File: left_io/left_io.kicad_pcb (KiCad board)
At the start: 8 copper layers, 70 x 185 mm, 266 parts, among them J190 AUX/SOLAR protected screw ter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, J21 USB-C dual-role data/PD port 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, J22 USB-C source-only data port J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, J23 USB-C source-only data port J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, J24 USB 3.0 Type-A internal heade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, J25 USB 2.0 Type-A internal heade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, Q15 SiSS4409DN 40V reverse-blocki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, Q16 SiSS4409DN 40V reverse-blocki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, Q17 SiSS4409DN 40V reverse-blocki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, Q18 SiSS4409DN 40V reverse-blocki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, Q2001 2N7002K DFP USB2 enable inver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, U14 LTC4418IUF#PBF dual-input PD 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, U1700 USB7206C-I/KDX six-port USB 3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, U1701 TPS62823DLC 3A USB7206C 1.146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, U1702 TLV803EA29 USB hub reset supe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, U1703 TPS56637RPAR VSYS to USB_PORT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, U1704 SN74LVC1G08 hub 3V3/core-PG r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, U1740 TPS2553DDBVR 1.3A USB branch, U1741 TPS25810RVCR Type-C DFP contr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, U1742 HD3SS6126RUAR USB3 orientatio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, U1743 TPD1S514-1YZR 5.9V VBUS OVP, U1745 TPD4E05U06 USB2/CC ESD, U1780 TPS2553DDBVR 1.3A USB branch, U1781 TPS25810RVCR Type-C DFP contr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, U1782 HD3SS6126RUAR USB3 orientatio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, U1783 TPD1S514-1YZR 5.9V VBUS OVP, U1785 TPD4E05U06 USB2/CC ESD, U1800 TPS2553DDBVR USB3-A VBUS bran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, U1801 USBLC6-2P6 USB3-A D+/D- ESD, U1802 TPD4E05U06 USB3-A SuperSpeed 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, U1803 TPS2553DDBVR USB2-A VBUS bran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, U1804 USBLC6-2P6 USB2-A D+/D- ESD, U2000 TUSB1142 USB 3.2 Gen 2 orient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, U2001 TPD4S201 CC and USB2 short-to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, U2002 CAT24C256 32KB private TPS257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, U2003 TS3USB30E DFP-qualified USB2 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, U2004 SN74LVC2G07 partial-power-dow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, U2005 TVS2200 22V USB VBUS surge cl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, U2006 SN74LVC1G08 DFP and attached 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, U41 TPS25751AD USB-PD DRP control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, U720 TPS26630RGER PD1 default-off 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, Y1700 25.000MHz 3.3V USB hub oscill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

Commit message: Board split Phase 4a: FPC connectors wired through the four split schematics
Connector symbols and sheets now exist in every project and the boundary
nets are pinned through them (same conductor order on both ends, verified
netlist-by-netlist):
  - gen/fpc_contract.py: authoritative FPC-1/2/3 pin maps + center-side
    renames (single source of truth for schematics, board pad nets, cable
    spec, and gate contracts)
  - gen/Conn_01x100_FFC_MP.kicad_sym (derived from the 30-pin pattern)
  - center: real fpc1_left/fpc2_right/fpc3_bms sheets wired to host pins
  - left_io/right_io: left_fpc/right_fpc connector sheets; bms carries
    FPC106 inline
  - connector refs FPC101..FPC106 (valid designators; FPC1_L-style refs
    broke KiCad annotation)
  - pack-rail naming reconciled: center gauge divider BAT_PROT_VIN ->
    PACK_POS_FUSED (same node as the BMS LTC4368 output); BMS ground
    /GND -> GND (pack negative is the system ground)

Boards: daughterboards re-synced from their connector-bearing schematics;
center connectors placed and their pad nets assigned text-side ((net
"name") convention).  Connector pads verified against every other
footprint (0 overlaps) and DRC shows 0 shorts on all four boards (center
16 pre-existing, down from 17).

Fixed two latent generator bugs exposed by the wiring:
  - resolve_connectors used naive +R rotation, placing Phase 3 connectors
    against mirrored phantom positions
  - pad half-extents were computed as footprint_rot+pad_rot, but KiCad
    saves pads with world orientation (FH12-100S pins are 1.3mm wide);
    both verified empirically against pcbnew, plus a connector-nudge pass
    for parts sandwiched between the connector body and pin columns

Gate: SCHEMATIC RELEASE CHECK: PASS (FPC pin contracts added per project;
closure audits 0 FAIL).  Routing remains manual (Phase 4b).
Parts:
- removed FPC1_L: FH12-100S-0.5SH_1x100-1MP_P0.50mm_Horizontal, ducktop2:FH12-100S-0.5SH_1x100-1MP_P0.50mm_Horizontal
- added FPC101: FH12-100S-0.5SH (FPC-1), ducktop2:FH12-100S-0.5SH_1x100-1MP_P0.50mm_Horizontal, F.Cu at (65.6, 130.5)
- moved R1840 54.0 mm to (8.00, 4.00)
- moved R1708 29.0 mm to (62.0, 2.00)
- moved U1702 15.0 mm to (39.0, 5.00)
- moved U1703 5.00 mm to (44.0, 5.00)
- moved U1701 4.12 mm to (24.0, 5.00)
- moved R2083 4.00 mm to (12.0, 4.00)
- moved R2084 4.00 mm to (16.0, 4.00)
- moved R2086 4.00 mm to (20.0, 4.00)

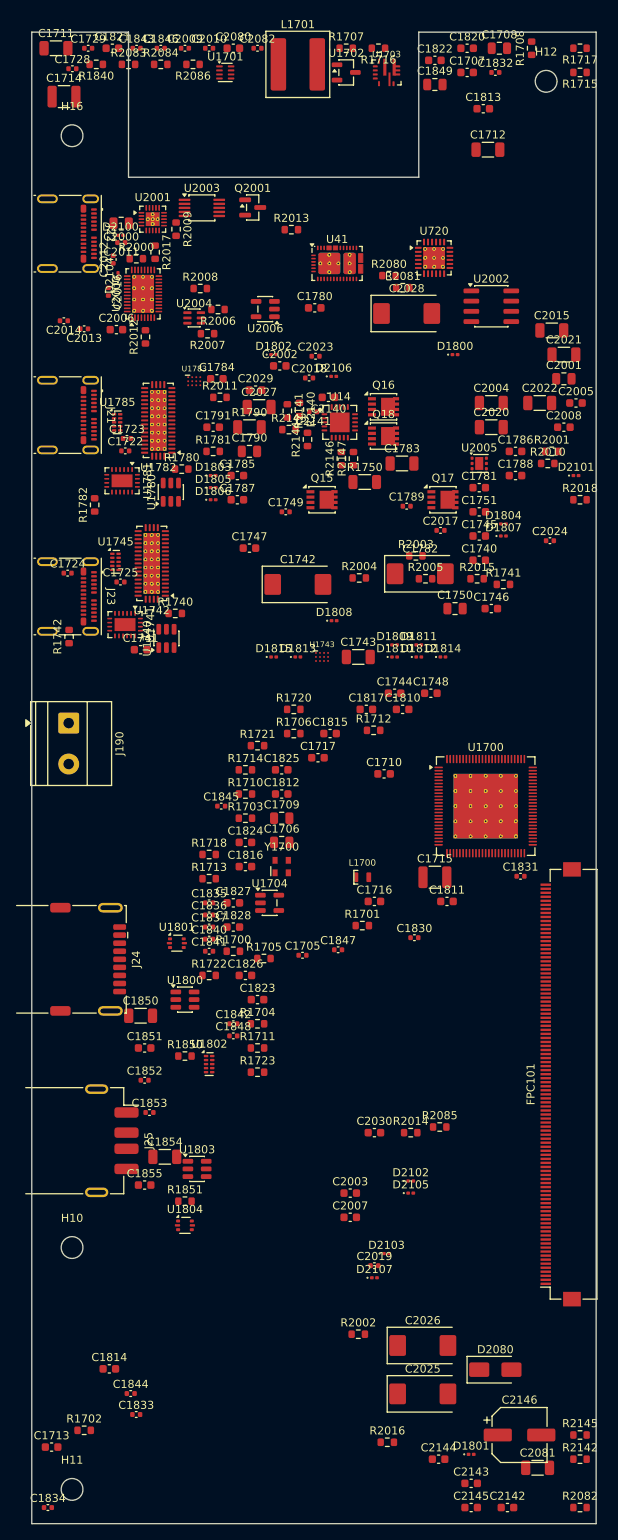
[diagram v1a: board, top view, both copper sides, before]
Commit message: Phase 4 deep audit: FH41-68S connectors, placement hygiene, one-shot fixes
Found and fixed four board-killers in the pre-fab audit:

1. Fictional connector: the Hirose FH12 series stops at 60 positions, so
   the 100-pin FH12-100S used for FPC-1/FPC-2 does not exist.  Replaced
   with the FH41-68S-0.5SH(05) (shielded-FFC, 68 positions; FPC-1 uses
   pins 1-53, FPC-2 pins 1-61):
   - new footprint derived from KiCad's FH41-30S (68 signal pads, MP at
     +/-18, 14 SH solder-holds, 38mm body) with SH pads tied to GND
   - new 68-pin symbol (Conn_01x68_FFC_MP), pin maps trimmed to 68
   - fictional FH12-100S footprint/symbol/script removed
   - cable spec updated (68-pin shielded FFC, one type for both)

2. Connector courtyard conflicts: parts sat under connector bodies
   (pads cleared, bodies collided).  Placement now enforces courtyard
   clearance against the connector body; the resolver scans with
   courtyard checks; a double-shift bug that hid re-placed parts' true
   positions was fixed.

3. FPC-3 orientation: the FH12's FPC enters from the +y side; both FPC-3
   connectors faced away from the seam.  FPC105 -> (123.5, 6.5) rot 180,
   FPC106 -> (30, 54) rot 0 so the cable exits the center bottom edge
   and enters the BMS top edge.

4. Original-layout defects: 16 genuine pad-pad shorts (inductor pads
   swallowing caps, passives on each other, parts on mounting holes) and
   23 parts inside the hinge cutouts (physically off the board) are all
   moved to legal spots; zones refilled against the final placement.

New post-build hygiene sweep (fix_board_hygiene.py) uses the final board
text as the geometry oracle, converges to a clean state, and reports
residuals instead of dropping them.

Final DRC: 0 shorts / 0 clearance / 0 hole violations on all four boards
(bms fully clean).  Remaining: courtyard touches around the Mu socket and
M.2 slot (design-inherent moat), chassis-edge copper, zone islands, silk
cosmetics, and unrouted nets (Phase 4b).  Gate: SCHEMATIC R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
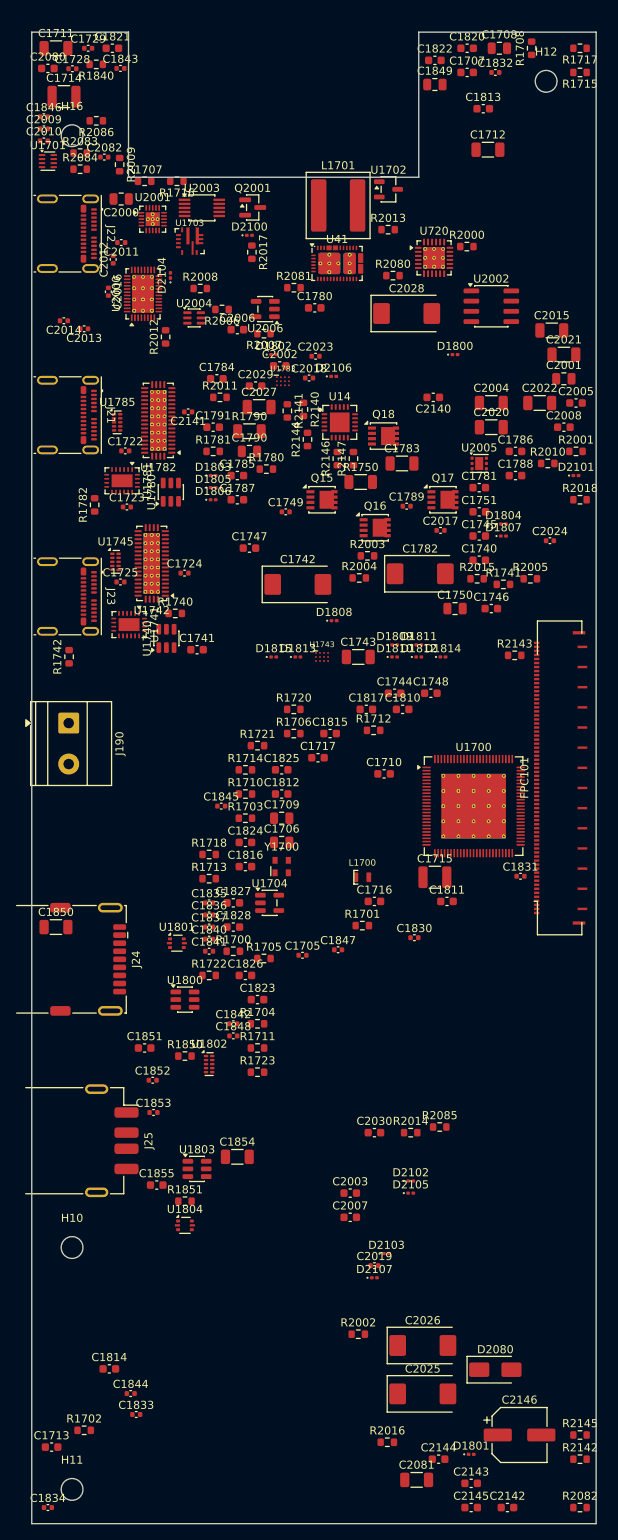
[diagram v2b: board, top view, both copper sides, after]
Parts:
- FPC101: value FH12-100S-0.5SH (FPC-1) -> FH41-68S-0.5SH (FPC-1); footprint ducktop2:FH12-100S-0.5SH_1x100-1MP_P0.50mm_Horizontal -> ducktop2:Hirose_FH41-68S-0.5SH_1x68_1MP_1SH_P0.5mm_Horizontal
- moved R2000 41.0 mm to (54.0, 26.6)
- moved R2143 39.6 mm to (59.9, 77.3)
- moved FPC101 38.0 mm to (65.6, 92.5)
- moved U1703 32.2 mm to (19.6, 25.9)
- moved R1707 30.0 mm to (14.0, 18.5)
- moved R1716 30.0 mm to (18.0, 18.5)
- moved U1701 24.6 mm to (2.00, 16.0)
- moved C2010 23.5 mm to (1.50, 13.5)
- moved C2082 23.3 mm to (9.00, 15.5)
- moved C2080 23.1 mm to (2.00, 4.50)
- moved C2009 20.2 mm to (1.50, 12.0)
- moved L1701 18.2 mm to (38.0, 21.5)
- moved C1846 16.8 mm to (1.50, 10.5)
- moved R2084 16.4 mm to (6.00, 17.0)
- moved D2100 16.0 mm to (27.0, 25.2)
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
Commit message: Phase 5: second-opinion audit remediation + rebuilt, verified board pipeline
Second-opinion AI audit found A-tier defects; remediation applied and the
board pipeline rebuilt on a known-good base with the fixes it needed:

- electrical: LTC4418IUF symbol pinout corrected (both selectors were
  dead as drawn); center charge cascade (U15 <- U15B, PD1 > PD2 > AUX);
  pack negative never crosses FPC-3, 15-pin FG_VSS return; power-budgeted
  FPC pin maps (0.4 A/pin derate); J12/DS4 completed; AUX source fuse
- FH41-68S footprint: 13 datasheet-correct SH pads + SH pin in symbol
- connector geometry settled against the Hirose FH12 2D drawing: FFC
  enters opposite the solder pins (mouth = local +Y); reversed side-B
  maps are correct for the 180-deg-mounted pairs; rotations set so mouths
  face across every seam
- pipeline (generate_split_boards.py): per-pin pad-net resync from the
  netlists (kills shadow nets for good), netlist-exact name
  normalization, netlist-only part injection (cascade, probe headers),
  zone refill after outline swap, read-before-write race fixed, orphan
  parts dropped loudly, non-zero exit on unresolved overlaps
- monolith board relocated to old/monolith_ducktop2.kicad_pcb (placement
  oracle for the center cut only)

verified end state: 4 boards 0 shorts / 0 clearance / 0 drill, 0 boundary
crossings, 6/6 connectors contract-exact with mouths facing, 0 shadow
nets, gates PASS x4, ERC 0 x4. routing next (499 nets/board).
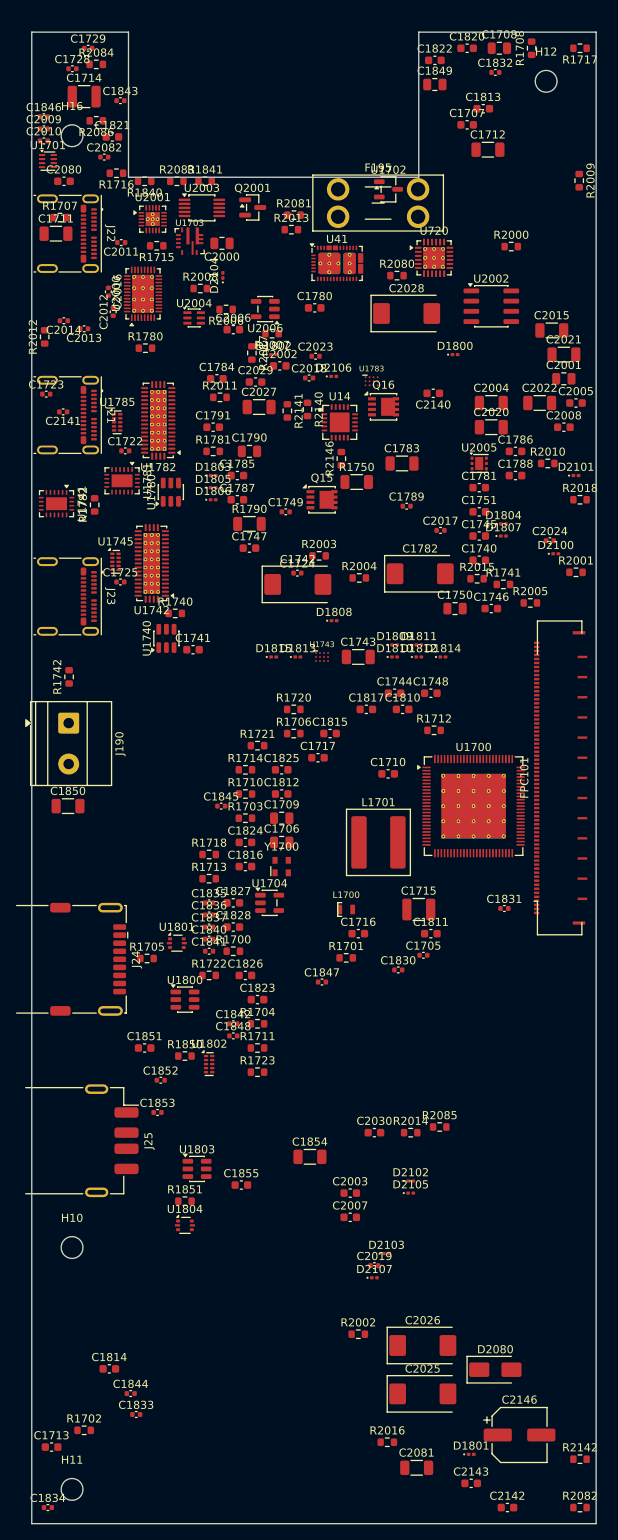
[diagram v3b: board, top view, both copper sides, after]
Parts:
- removed C2144, C2145: 100n 50V selector local, Capacitor_SMD:C_0603_1608Metric
- removed Q17, Q18: SiSS4409DN 40V reverse-blocking PMOS, Package_SO:Vishay_PowerPAK_1212-8_Single
- removed R2143: 1.00M 0.1% 15V UV top, Resistor_SMD:R_0603_1608Metric
- removed R2144: 19.6k 0.1% 15V window middle, Resistor_SMD:R_0603_1608Metric
- removed R2145: 63.4k 0.1% 15V OV bottom, Resistor_SMD:R_0603_1608Metric
- removed R2147: 10k PD2 VALID pull-up, Resistor_SMD:R_0603_1608Metric
- added F195: 3A MINI AUX source fuse: Littelfuse 0297003.WXNV, Fuse:Fuseholder_Blade_Mini_Keystone_3568, F.Cu at (38.0, 19.5)
- added R1841: 10k DS4 PRT_CTL idle pull-up (J12 branch enable, remote), Resistor_SMD:R_0603_1608Metric, F.Cu at (21.5, 18.5)
- H10, H11, H12, H16: value MountingHole_2.7mm_M2.5 -> M2.5 isolated mainboard mounting hole
- U14: value LTC4418IUF#PBF dual-input PD selector -> LTC4418IUF#PBF dual-input PD selector (V1 = J21)
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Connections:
- net HUB_3V3_OK renamed /USB Hub + Ports/HUB_3V3_OK
- net HUB_BC_EN renamed /USB Hub + Ports/HUB_BC_EN
- net HUB_CFG1 renamed /USB Hub + Ports/HUB_CFG1
- net HUB_CFG2 renamed /USB Hub + Ports/HUB_CFG2
- net HUB_CFG3 renamed /USB Hub + Ports/HUB_CFG3
- net HUB_CLK renamed /USB Hub + Ports/HUB_CLK
- net HUB_CORE_FB renamed /USB Hub + Ports/HUB_CORE_FB
- net HUB_CORE_PG renamed /USB Hub + Ports/HUB_CORE_PG
- net HUB_CORE_SW renamed /USB Hub + Ports/HUB_CORE_SW
- net HUB_DIS5_DM renamed /USB Hub + Ports/HUB_DIS5_DM
- net HUB_DIS5_DP renamed /USB Hub + Ports/HUB_DIS5_DP
- net HUB_DIS5_RX_N renamed /USB Hub + Ports/HUB_DIS5_RX_N
- net HUB_DIS5_RX_P renamed /USB Hub + Ports/HUB_DIS5_RX_P
- net HUB_DIS5_TX_N renamed /USB Hub + Ports/HUB_DIS5_TX_N
- net HUB_DIS5_TX_P renamed /USB Hub + Ports/HUB_DIS5_TX_P
- net HUB_DIS6_DM renamed /USB Hub + Ports/HUB_DIS6_DM
- net HUB_DIS6_DP renamed /USB Hub + Ports/HUB_DIS6_DP
- net HUB_DS1_PRT_CTL renamed /USB Hub + Ports/HUB_DS1_PRT_CTL
- net HUB_DS2_DM renamed /USB Hub + Ports/HUB_DS2_DM
- net HUB_DS2_DP renamed /USB Hub + Ports/HUB_DS2_DP
- net HUB_DS2_SSRX_N renamed /USB Hub + Ports/HUB_DS2_SSRX_N
- net HUB_DS2_SSRX_P renamed /USB Hub + Ports/HUB_DS2_SSRX_P
- net HUB_DS2_SSTX_N renamed /USB Hub + Ports/HUB_DS2_SSTX_N
- net HUB_DS2_SSTX_P renamed /USB Hub + Ports/HUB_DS2_SSTX_P
- net HUB_DS2_TX_RAW_N renamed /USB Hub + Ports/HUB_DS2_TX_RAW_N
- net HUB_DS2_TX_RAW_P renamed /USB Hub + Ports/HUB_DS2_TX_RAW_P
- net HUB_DS3_DM renamed /USB Hub + Ports/HUB_DS3_DM
- net HUB_DS3_DP renamed /USB Hub + Ports/HUB_DS3_DP
- net HUB_DS3_SSRX_N renamed /USB Hub + Ports/HUB_DS3_SSRX_N
- net HUB_DS3_SSRX_P renamed /USB Hub + Ports/HUB_DS3_SSRX_P
- net HUB_DS3_SSTX_N renamed /USB Hub + Ports/HUB_DS3_SSTX_N
- net HUB_DS3_SSTX_P renamed /USB Hub + Ports/HUB_DS3_SSTX_P
- net HUB_DS3_TX_RAW_N renamed /USB Hub + Ports/HUB_DS3_TX_RAW_N
- net HUB_DS3_TX_RAW_P renamed /USB Hub + Ports/HUB_DS3_TX_RAW_P
- net HUB_NON_REM renamed /USB Hub + Ports/HUB_NON_REM
- net HUB_PRT_CTL2 renamed /USB Hub + Ports/HUB_PRT_CTL2
- net HUB_PRT_CTL3 renamed /USB Hub + Ports/HUB_PRT_CTL3
- net HUB_RBIAS renamed /USB Hub + Ports/HUB_RBIAS
- net HUB_RESET_N renamed /USB Hub + Ports/HUB_RESET_N
- net HUB_SPI_CLK renamed /USB Hub + Ports/HUB_SPI_CLK
- net HUB_SPI_D1 renamed /USB Hub + Ports/HUB_SPI_D1
- net HUB_SPI_D2 renamed /USB Hub + Ports/HUB_SPI_D2
- net HUB_SPI_D3 renamed /USB Hub + Ports/HUB_SPI_D3
- net HUB_TEST1 renamed /USB Hub + Ports/HUB_TEST1
- net HUB_TEST2 renamed /USB Hub + Ports/HUB_TEST2
- net HUB_TEST3 renamed /USB Hub + Ports/HUB_TEST3
- net HUB_UP_TX_RAW_N renamed /USB Hub + Ports/HUB_UP_TX_RAW_N
- net HUB_UP_TX_RAW_P renamed /USB Hub + Ports/HUB_UP_TX_RAW_P
- net HUB_VCORE renamed /USB Hub + Ports/HUB_VCORE
- net J22_5V_PRE renamed /USB Hub + Ports/J22_5V_PRE
- net J22_CC1 renamed /USB Hub + Ports/J22_CC1
- net J22_CC2 renamed /USB Hub + Ports/J22_CC2
- net J22_ILIM renamed /USB Hub + Ports/J22_ILIM
- net J22_POL_N renamed /USB Hub + Ports/J22_POL_N
- net J22_REF renamed /USB Hub + Ports/J22_REF
- net J22_REF_RTN renamed /USB Hub + Ports/J22_REF_RTN
- net J22_RX1_N renamed /USB Hub + Ports/J22_RX1_N
- net J22_RX1_P renamed /USB Hub + Ports/J22_RX1_P
- net J22_RX2_N renamed /USB Hub + Ports/J22_RX2_N
- net J22_RX2_P renamed /USB Hub + Ports/J22_RX2_P
- net J22_TX1_N renamed /USB Hub + Ports/J22_TX1_N
- net J22_TX1_P renamed /USB Hub + Ports/J22_TX1_P
- net J22_TX2_N renamed /USB Hub + Ports/J22_TX2_N
- net J22_TX2_P renamed /USB Hub + Ports/J22_TX2_P
- net J22_VBUS renamed /USB Hub + Ports/J22_VBUS
- net J22_VBUS_POWER renamed /USB Hub + Ports/J22_VBUS_POWER
- net J22_VBUS_SYS renamed /USB Hub + Ports/J22_VBUS_SYS
- net J23_5V_PRE renamed /USB Hub + Ports/J23_5V_PRE
- net J23_CC1 renamed /USB Hub + Ports/J23_CC1
- net J23_CC2 renamed /USB Hub + Ports/J23_CC2
- net J23_ILIM renamed /USB Hub + Ports/J23_ILIM
- net J23_POL_N renamed /USB Hub + Ports/J23_POL_N
- net J23_REF renamed /USB Hub + Ports/J23_REF
- net J23_REF_RTN renamed /USB Hub + Ports/J23_REF_RTN
- net J23_RX1_N renamed /USB Hub + Ports/J23_RX1_N
- net J23_RX1_P renamed /USB Hub + Ports/J23_RX1_P
- net J23_RX2_N renamed /USB Hub + Ports/J23_RX2_N
- net J23_RX2_P renamed /USB Hub + Ports/J23_RX2_P
- net J23_TX1_N renamed /USB Hub + Ports/J23_TX1_N
- net J23_TX1_P renamed /USB Hub + Ports/J23_TX1_P
- net J23_TX2_N renamed /USB Hub + Ports/J23_TX2_N
- net J23_TX2_P renamed /USB Hub + Ports/J23_TX2_P
- net J23_VBUS renamed /USB Hub + Ports/J23_VBUS
- net J23_VBUS_POWER renamed /USB Hub + Ports/J23_VBUS_POWER
- net J23_VBUS_SYS renamed /USB Hub + Ports/J23_VBUS_SYS
- net J24_5V_PRE renamed /USB Hub + Ports/J24_5V_PRE
- net J24_ILIM renamed /USB Hub + Ports/J24_ILIM
- net J24_SSTX_N renamed /USB Hub + Ports/J24_SSTX_N
- net J24_SSTX_P renamed /USB Hub + Ports/J24_SSTX_P
- net J25_5V_PRE renamed /USB Hub + Ports/J25_5V_PRE
- net J25_ILIM renamed /USB Hub + Ports/J25_ILIM
- net PD1_CC1_CONN renamed /PD1 Dual-Role/PD1_CC1_CONN
- net PD1_CC1_SYS renamed /PD1 Dual-Role/PD1_CC1_SYS
- net PD1_CC2_CONN renamed /PD1 Dual-Role/PD1_CC2_CONN
- net PD1_CC2_SYS renamed /PD1 Dual-Role/PD1_CC2_SYS
- net PD1_CC_ESD_VBIAS renamed /PD1 Dual-Role/PD1_CC_ESD_VBIAS
- net PD1_CC_FAULT_LOCAL_N renamed /PD1 Dual-Role/PD1_CC_FAULT_LOCAL_N
- net PD1_CTX1_RAW_N renamed /PD1 Dual-Role/PD1_CTX1_RAW_N
- net PD1_CTX1_RAW_P renamed /PD1 Dual-Role/PD1_CTX1_RAW_P
- net PD1_CTX2_RAW_N renamed /PD1 Dual-Role/PD1_CTX2_RAW_N
- net PD1_CTX2_RAW_P renamed /PD1 Dual-Role/PD1_CTX2_RAW_P
- net PD1_DM_CONN renamed /PD1 Dual-Role/PD1_DM_CONN
- net PD1_DM_HOST_SWITCHED renamed /PD1 Dual-Role/PD1_DM_HOST_SWITCHED
- net PD1_DP_CONN renamed /PD1 Dual-Role/PD1_DP_CONN
- net PD1_DP_HOST_SWITCHED renamed /PD1 Dual-Role/PD1_DP_HOST_SWITCHED
- net PD1_DRAIN_THERMAL renamed /PD1 Dual-Role/PD1_DRAIN_THERMAL
- net PD1_EEPROM_IRQ_N renamed /PD1 Dual-Role/PD1_EEPROM_IRQ_N
- net PD1_EEPROM_SCL renamed /PD1 Dual-Role/PD1_EEPROM_SCL
- net PD1_EEPROM_SDA renamed /PD1 Dual-Role/PD1_EEPROM_SDA
- net PD1_EFUSE_DVDT renamed /PD1 Dual-Role/PD1_EFUSE_DVDT
- net PD1_EFUSE_ILIM renamed /PD1 Dual-Role/PD1_EFUSE_ILIM
- net PD1_EFUSE_OV renamed /PD1 Dual-Role/PD1_EFUSE_OV
- net PD1_EFUSE_SHDN renamed /PD1 Dual-Role/PD1_EFUSE_SHDN
- net PD1_EFUSE_UV renamed /PD1 Dual-Role/PD1_EFUSE_UV
- net PD1_GPIO_ATTACH renamed /PD1 Dual-Role/PD1_GPIO_ATTACH
- net PD1_GPIO_DFP renamed /PD1 Dual-Role/PD1_GPIO_DFP
- net PD1_GPIO_FLIP renamed /PD1 Dual-Role/PD1_GPIO_FLIP
- net PD1_HOST_ATTACHED renamed /PD1 Dual-Role/PD1_HOST_ATTACHED
- net PD1_LDO1V5 renamed /PD1 Dual-Role/PD1_LDO1V5
- net PD1_LDO3V3 renamed /PD1 Dual-Role/PD1_LDO3V3
- net PD1_MUX_EN renamed /PD1 Dual-Role/PD1_MUX_EN
- net PD1_MUX_EQCFG renamed /PD1 Dual-Role/PD1_MUX_EQCFG
- net PD1_MUX_FLIP renamed /PD1 Dual-Role/PD1_MUX_FLIP
- net PD1_MUX_MODE renamed /PD1 Dual-Role/PD1_MUX_MODE
- net PD1_MUX_SLEEP_N renamed /PD1 Dual-Role/PD1_MUX_SLEEP_N
- net PD1_MUX_SSEQ1 renamed /PD1 Dual-Role/PD1_MUX_SSEQ1
- net PD1_MUX_VIO renamed /PD1 Dual-Role/PD1_MUX_VIO
- net PD1_PPHV renamed /PD1 Dual-Role/PD1_PPHV
- net PD1_RX1_N renamed /PD1 Dual-Role/PD1_RX1_N
- net PD1_RX1_P renamed /PD1 Dual-Role/PD1_RX1_P
- net PD1_RX2_N renamed /PD1 Dual-Role/PD1_RX2_N
- net PD1_RX2_P renamed /PD1 Dual-Role/PD1_RX2_P
- net PD1_SEL_FET_COMMON renamed /PD1 Dual-Role/PD1_SEL_FET_COMMON
- net PD1_SEL_GATE renamed /PD1 Dual-Role/PD1_SEL_GATE
- net PD1_SEL_OV renamed /PD1 Dual-Role/PD1_SEL_OV
- net PD1_SEL_UV renamed /PD1 Dual-Role/PD1_SEL_UV
- net PD1_SSRX_RAW_N renamed /PD1 Dual-Role/PD1_SSRX_RAW_N
- net PD1_SSRX_RAW_P renamed /PD1 Dual-Role/PD1_SSRX_RAW_P
- net PD1_TX1_N renamed /PD1 Dual-Role/PD1_TX1_N
- net PD1_TX1_P renamed /PD1 Dual-Role/PD1_TX1_P
- net PD1_TX2_N renamed /PD1 Dual-Role/PD1_TX2_N
- net PD1_TX2_P renamed /PD1 Dual-Role/PD1_TX2_P
- net PD1_USB2_OE_N renamed /PD1 Dual-Role/PD1_USB2_OE_N
- net PD1_VBUS_GATED renamed /PD1 Dual-Role/PD1_VBUS_GATED
- net PD_SEL_TMR renamed /PD1 Dual-Role/PD_SEL_TMR
- net USB5_BOOT renamed /USB Hub + Ports/USB5_BOOT
- net USB5_EN renamed /USB Hub + Ports/USB5_EN
- net USB5_FB renamed /USB Hub + Ports/USB5_FB
- net USB5_PG renamed /USB Hub + Ports/USB5_PG
- net USB5_SW renamed /USB Hub + Ports/USB5_SW
- C1706 pad 1: SYS_3V3 -> /SYS_3V3
- C1707 pad 1: SYS_3V3 -> /SYS_3V3
- C1711 pad 1: VSYS -> /VSYS
- C1712 pad 1: VSYS -> /VSYS
- C1713 pad 1: VSYS -> /VSYS
- C1714 pad 1: USB_PORT_5V -> /USB_PORT_5V
- C1715 pad 1: USB_PORT_5V -> /USB_PORT_5V
- C1716 pad 1: SYS_3V3 -> /SYS_3V3
- C1717 pad 1: SYS_3V3 -> /SYS_3V3
- C1728 pad 2: USBC2_SSRX_P -> /USBC2_SSRX_P
- C1729 pad 2: USBC2_SSRX_N -> /USBC2_SSRX_N
- C1740 pad 1: USB_PORT_5V -> /USB_PORT_5V
- C1744 pad 1: SYS_3V3 -> /SYS_3V3
- C1745 pad 1: SYS_3V3 -> /SYS_3V3
- C1746 pad 1: SYS_3V3 -> /SYS_3V3
- C1747 pad 1: SYS_3V3 -> /SYS_3V3
- C1748 pad 1: SYS_3V3 -> /SYS_3V3
- C1749 pad 1: SYS_3V3 -> /SYS_3V3
- C1780 pad 1: USB_PORT_5V -> /USB_PORT_5V
- C1784 pad 1: SYS_3V3 -> /SYS_3V3
- C1785 pad 1: SYS_3V3 -> /SYS_3V3
- C1786 pad 1: SYS_3V3 -> /SYS_3V3
- C1787 pad 1: SYS_3V3 -> /SYS_3V3
- C1788 pad 1: SYS_3V3 -> /SYS_3V3
- C1789 pad 1: SYS_3V3 -> /SYS_3V3
- C1810 pad 1: SYS_3V3 -> /SYS_3V3
- C1811 pad 1: SYS_3V3 -> /SYS_3V3
- C1812 pad 1: SYS_3V3 -> /SYS_3V3
- C1813 pad 1: SYS_3V3 -> /SYS_3V3
- C1814 pad 1: SYS_3V3 -> /SYS_3V3
- C1815 pad 1: SYS_3V3 -> /SYS_3V3
- C1816 pad 1: SYS_3V3 -> /SYS_3V3
- C1817 pad 1: SYS_3V3 -> /SYS_3V3
- C1830 pad 1: SYS_3V3 -> /SYS_3V3
- C1831 pad 1: SYS_3V3 -> /SYS_3V3
- C1832 pad 1: SYS_3V3 -> /SYS_3V3
- C1833 pad 1: SYS_3V3 -> /SYS_3V3
- C1834 pad 1: SYS_3V3 -> /SYS_3V3
- C1835 pad 1: SYS_3V3 -> /SYS_3V3
- C1836 pad 1: SYS_3V3 -> /SYS_3V3
- C1837 pad 1: SYS_3V3 -> /SYS_3V3
- C1849 pad 1: SYS_3V3 -> /SYS_3V3
- C2003 pad 1: SYS_3V3 -> /SYS_3V3
- C2004 pad 1: SYS_3V3 -> /SYS_3V3
- C2005 pad 1: SYS_3V3 -> /SYS_3V3
- C2006 pad 1: SYS_3V3 -> /SYS_3V3
- C2007 pad 1: SYS_3V3 -> /SYS_3V3
- C2008 pad 1: SYS_3V3 -> /SYS_3V3
- C2009 pad 2: USBC1_SSRX_P -> /USBC1_SSRX_P
- C2010 pad 2: USBC1_SSRX_N -> /USBC1_SSRX_N
- C2015 pad 1: PD1_VBUS_RAW -> /PD1_VBUS_RAW
- C2016 pad 1: PD1_VBUS_RAW -> /PD1_VBUS_RAW
- C2017 pad 1: PD1_VBUS_RAW -> /PD1_VBUS_RAW
- C2018 pad 1: PD1_VBUS_RAW -> /PD1_VBUS_RAW
- C2019 pad 1: PD1_VBUS_RAW -> /PD1_VBUS_RAW
- C2022 pad 1: MCU_3V3 -> /MCU_3V3
- C2025 pad 1: USB_PORT_5V -> /USB_PORT_5V
- C2026 pad 1: USB_PORT_5V -> /USB_PORT_5V
- C2027 pad 1: USB_PORT_5V -> /USB_PORT_5V
- C2030 pad 1: SYS_3V3 -> /SYS_3V3
- C2140 pad 1: PD_SEL_INTVCC -> /PD1 Dual-Role/PD_SEL_INTVCC
- C2146 pad 1: USB_PD_SELECTED -> /USB_PD_SELECTED
- FPC101 pad 1: VSYS -> /VSYS
- FPC101 pad 10: GND -> /USB_PORT_5V
- FPC101 pad 11: PD1_VBUS_RAW -> /USB_PORT_5V
- FPC101 pad 12: GND -> /USB_PORT_5V
- FPC101 pad 13: AUX_DC_RAW -> GND
- FPC101 pad 14: GND -> /SYS_3V3
- FPC101 pad 15: USB_PD_SELECTED -> /SYS_3V3
- FPC101 pad 16: GND -> /MCU_3V3
- FPC101 pad 17: INTERNAL_USB_VBUS_VALID -> /PD1_VBUS_RAW
- FPC101 pad 18: GND -> /PD1_VBUS_RAW
- FPC101 pad 19: PD1_I2C_SCL -> /PD1_VBUS_RAW
- FPC101 pad 2: VSYS -> /VSYS
- FPC101 pad 20: PD1_I2C_SDA -> /PD1_VBUS_RAW
- FPC101 pad 21: GND -> /PD1_VBUS_RAW
- FPC101 pad 22: PD1_TCPC_IRQ_N -> /PD1_VBUS_RAW
- FPC101 pad 23: GND -> /USB_PD_SELECTED
- FPC101 pad 24: PD1_PATH_EN -> /USB_PD_SELECTED
- FPC101 pad 25: GND -> /USB_PD_SELECTED
- FPC101 pad 26: PD1_VALID_N -> /USB_PD_SELECTED
- FPC101 pad 27: GND -> /USB_PD_SELECTED
- FPC101 pad 28: PD2_VALID_N -> /USB_PD_SELECTED
- FPC101 pad 29: GND -> /AUX_DC_RAW
- FPC101 pad 3: GND -> /VSYS
- FPC101 pad 30: PD1_EFUSE_FAULT_N -> /AUX_DC_RAW
- FPC101 pad 31: GND -> /AUX_DC_RAW
- FPC101 pad 32: PD_PROTECT_FAULT_N -> /AUX_DC_RAW
- FPC101 pad 33: GND -> /AUX_DC_RAW
- FPC101 pad 34: USBC1_DP -> /AUX_DC_RAW
- FPC101 pad 35: USBC1_DM -> GND
- FPC101 pad 37: USBC2_DP -> GND
- FPC101 pad 38: USBC2_DM -> /INTERNAL_USB_VBUS_VALID
- FPC101 pad 39: GND -> /PD1_I2C_SCL
- FPC101 pad 4: USB_PORT_5V -> /VSYS
- FPC101 pad 40: HUB_DS1_DP -> /PD1_I2C_SDA
- FPC101 pad 41: HUB_DS1_DM -> /PD1_TCPC_IRQ_N
- FPC101 pad 42: GND -> /PD1_PATH_EN
- FPC101 pad 43: USBC1_SSRX_P -> /PD1_VALID_N
- FPC101 pad 44: USBC1_SSRX_N -> /PD1_EFUSE_FAULT_N
- FPC101 pad 45: GND -> /PD_PROTECT_FAULT_N
- FPC101 pad 46: USBC1_SSTX_P -> /HUB_DS4_DP
- FPC101 pad 47: USBC1_SSTX_N -> /HUB_DS4_DM
- FPC101 pad 48: GND -> /HUB_PRT_CTL4
- FPC101 pad 49: USBC2_SSRX_P -> /USBC1_DP
- FPC101 pad 5: USB_PORT_5V -> /VSYS
- FPC101 pad 50: USBC2_SSRX_N -> /USBC1_DM
- FPC101 pad 52: USBC2_SSTX_P -> /USBC2_DP
- FPC101 pad 53: USBC2_SSTX_N -> /USBC2_DM
- FPC101 pad 55: GND -> /HUB_DS1_DP
- FPC101 pad 56: GND -> /HUB_DS1_DM
- FPC101 pad 58: GND -> /USBC1_SSRX_P
- FPC101 pad 59: GND -> /USBC1_SSRX_N
- FPC101 pad 6: GND -> /VSYS
- FPC101 pad 61: GND -> /USBC1_SSTX_P
- FPC101 pad 62: GND -> /USBC1_SSTX_N
- FPC101 pad 64: GND -> /USBC2_SSRX_P
- FPC101 pad 65: GND -> /USBC2_SSRX_N
- FPC101 pad 66: GND -> /USBC2_SSTX_P
- FPC101 pad 67: GND -> /USBC2_SSTX_N
- FPC101 pad 7: SYS_3V3 -> GND
- FPC101 pad 9: MCU_3V3 -> /USB_PORT_5V
- J190 pad 1: AUX_DC_RAW -> /PD1 Dual-Role/AUX_DC_TERM
- J21 pad A4: PD1_VBUS_RAW -> /PD1_VBUS_RAW
- J21 pad A8: (no net) -> unconnected-(J21-SBU1-PadA8)
- J21 pad A9: PD1_VBUS_RAW -> /PD1_VBUS_RAW
- J21 pad B4: PD1_VBUS_RAW -> /PD1_VBUS_RAW
- J21 pad B8: (no net) -> unconnected-(J21-SBU2-PadB8)
- J21 pad B9: PD1_VBUS_RAW -> /PD1_VBUS_RAW
- J22 pad A8: (no net) -> unconnected-(J22-SBU1-PadA8)
- J22 pad B8: (no net) -> unconnected-(J22-SBU2-PadB8)
- J23 pad A8: (no net) -> unconnected-(J23-SBU1-PadA8)
- J23 pad B8: (no net) -> unconnected-(J23-SBU2-PadB8)
- L1701 pad 2: USB_PORT_5V -> /USB_PORT_5V
- Q16 pad 5: USB_PD_SELECTED -> /USB_PD_SELECTED
- R1707 pad 1: SYS_3V3 -> /SYS_3V3
- R1710 pad 1: VSYS -> /VSYS
- R1712 pad 1: USB_PORT_5V -> /USB_PORT_5V
- R1714 pad 1: SYS_3V3 -> /SYS_3V3
- R1715 pad 1: SYS_3V3 -> /SYS_3V3
- R1716 pad 1: SYS_3V3 -> /SYS_3V3
- R1717 pad 1: SYS_3V3 -> /SYS_3V3
- R1718 pad 1: SYS_3V3 -> /SYS_3V3
- R1741 pad 1: SYS_3V3 -> /SYS_3V3
- R1781 pad 1: SYS_3V3 -> /SYS_3V3
- R1840 pad 1: SYS_3V3 -> /SYS_3V3
- R2000 pad 1: MCU_3V3 -> /MCU_3V3
- R2000 pad 2: PD_PROTECT_FAULT_N -> /PD_PROTECT_FAULT_N
- R2003 pad 1: MCU_3V3 -> /MCU_3V3
- R2003 pad 2: PD1_I2C_SDA -> /PD1_I2C_SDA
- R2004 pad 1: MCU_3V3 -> /MCU_3V3
- R2004 pad 2: PD1_I2C_SCL -> /PD1_I2C_SCL
- R2005 pad 1: MCU_3V3 -> /MCU_3V3
- R2005 pad 2: PD1_TCPC_IRQ_N -> /PD1_TCPC_IRQ_N
- R2006 pad 1: SYS_3V3 -> /SYS_3V3
- R2007 pad 1: SYS_3V3 -> /SYS_3V3
- R2012 pad 1: SYS_3V3 -> /SYS_3V3
- R2016 pad 1: SYS_3V3 -> /SYS_3V3
- R2017 pad 2: PD_PROTECT_FAULT_N -> /PD_PROTECT_FAULT_N
- R2085 pad 1: PD1_PATH_EN -> /PD1_PATH_EN
- R2086 pad 1: MCU_3V3 -> /MCU_3V3
- R2086 pad 2: PD1_EFUSE_FAULT_N -> /PD1_EFUSE_FAULT_N
- R2146 pad 1: MCU_3V3 -> /MCU_3V3
- R2146 pad 2: PD1_VALID_N -> /PD1_VALID_N
- U14 pad 10: PD2_VALID_N -> /PD1 Dual-Role/PD_SEL_INTVCC
- U14 pad 11: PD2_SEL_GATE -> unconnected-(U14-G2-Pad11)
- U14 pad 12: PD2_SEL_FET_COMMON -> GND
- U14 pad 15: USB_PD_SELECTED -> /USB_PD_SELECTED
- U14 pad 16: PD2_VBUS_GATED -> GND
- U14 pad 18: PD_SEL_INTVCC -> /PD1 Dual-Role/PD_SEL_INTVCC
- U14 pad 19: PD_SEL_INTVCC -> /PD1 Dual-Role/PD_SEL_INTVCC
- U14 pad 4: PD2_SEL_UV -> GND
- U14 pad 5: PD2_SEL_OV -> GND
- U14 pad 6: (no net) -> /PD1_VALID_N
- U14 pad 7: GND -> unconnected-(U14-~{VALID2}-Pad7)
- U14 pad 8: PD_SEL_INTVCC -> GND
- U14 pad 9: PD1_VALID_N -> unconnected-(U14-CAS-Pad9)
- U1700 pad 10: (no net) -> unconnected-(U1700B-RXDP1-Pad10)
- U1700 pad 11: (no net) -> unconnected-(U1700B-RXDM1-Pad11)
- U1700 pad 12: (no net) -> unconnected-(U1700B-NC-Pad12)
- U1700 pad 13: (no net) -> unconnected-(U1700B-NC-Pad13)
- U1700 pad 2: INTERNAL_USB_VBUS_VALID -> /INTERNAL_USB_VBUS_VALID
- U1700 pad 26: SYS_3V3 -> /SYS_3V3
- U1700 pad 3: (no net) -> unconnected-(U1700A-PF31-Pad3)
- U1700 pad 34: HUB_DS4_DP -> /HUB_DS4_DP
- U1700 pad 35: HUB_DS4_DM -> /HUB_DS4_DM
- U1700 pad 36: (no net) -> unconnected-(U1700C-TXDP4-Pad36)
- U1700 pad 37: (no net) -> unconnected-(U1700C-TXDM4-Pad37)
- U1700 pad 39: (no net) -> unconnected-(U1700C-RXDP4-Pad39)
- U1700 pad 4: (no net) -> unconnected-(U1700A-NC-Pad4)
- U1700 pad 40: (no net) -> unconnected-(U1700C-RXDM4-Pad40)
- U1700 pad 43: SYS_3V3 -> /SYS_3V3
- U1700 pad 44: (no net) -> unconnected-(U1700A-PF3-Pad44)
- U1700 pad 45: (no net) -> unconnected-(U1700A-PF4-Pad45)
- U1700 pad 46: (no net) -> unconnected-(U1700A-PF5-Pad46)
- U1700 pad 47: (no net) -> unconnected-(U1700A-PF6-Pad47)
- U1700 pad 48: (no net) -> unconnected-(U1700A-PF7-Pad48)
- U1700 pad 49: (no net) -> unconnected-(U1700A-PF8-Pad49)
- U1700 pad 5: HUB_DS1_DP -> /HUB_DS1_DP
- U1700 pad 50: (no net) -> unconnected-(U1700A-PF9-Pad50)
- U1700 pad 51: (no net) -> unconnected-(U1700A-PF10-Pad51)
- U1700 pad 52: (no net) -> unconnected-(U1700A-PF11-Pad52)
- U1700 pad 53: SYS_3V3 -> /SYS_3V3
- U1700 pad 54: (no net) -> unconnected-(U1700A-PF12-Pad54)
- U1700 pad 56: (no net) -> unconnected-(U1700A-PF13-Pad56)
- U1700 pad 57: HUB_PRT_CTL4 -> /HUB_PRT_CTL4
- U1700 pad 6: HUB_DS1_DM -> /HUB_DS1_DM
- U1700 pad 61: (no net) -> unconnected-(U1700A-PF18-Pad61)
- U1700 pad 62: SYS_3V3 -> /SYS_3V3
- U1700 pad 66: (no net) -> unconnected-(U1700A-PF19-Pad66)
- U1700 pad 67: SYS_3V3 -> /SYS_3V3
- U1700 pad 7: (no net) -> unconnected-(U1700B-TXDP1-Pad7)
- U1700 pad 74: (no net) -> unconnected-(U1700A-PF29-Pad74)
- U1700 pad 75: (no net) -> unconnected-(U1700A-PF26-Pad75)
- U1700 pad 76: (no net) -> unconnected-(U1700A-PF27-Pad76)
- U1700 pad 77: (no net) -> unconnected-(U1700A-PF28-Pad77)
- U1700 pad 79: SYS_3V3 -> /SYS_3V3
- U1700 pad 8: (no net) -> unconnected-(U1700B-TXDM1-Pad8)
- U1700 pad 80: (no net) -> unconnected-(U1700A-NC-Pad80)
- U1700 pad 88: SYS_3V3 -> /SYS_3V3
- U1700 pad 89: USBC2_DP -> /USBC2_DP
- U1700 pad 90: USBC2_DM -> /USBC2_DM
- U1700 pad 94: USBC2_SSTX_P -> /USBC2_SSTX_P
- U1700 pad 95: USBC2_SSTX_N -> /USBC2_SSTX_N
- U1700 pad 96: (no net) -> unconnected-(U1700A-ATEST-Pad96)
- U1700 pad 97: (no net) -> unconnected-(U1700A-XTALO-Pad97)
- U1700 pad 99: SYS_3V3 -> /SYS_3V3
- U1701 pad 1: SYS_3V3 -> /SYS_3V3
- U1701 pad 4: (no net) -> unconnected-(U1701-NC-Pad4)
- U1701 pad 7: SYS_3V3 -> /SYS_3V3
- U1702 pad 3: SYS_3V3 -> /SYS_3V3
- U1703 pad 5: (no net) -> unconnected-(U1703-NC-Pad5)
- U1703 pad 8: VSYS -> /VSYS
- U1704 pad 5: SYS_3V3 -> /SYS_3V3
- U1740 pad 1: USB_PORT_5V -> /USB_PORT_5V
- U1741 pad 16: (no net) -> unconnected-(U1741-~{DEBUG}-Pad16)
- U1741 pad 17: (no net) -> unconnected-(U1741-~{AUDIO}-Pad17)
- U1741 pad 19: (no net) -> unconnected-(U1741-~{UFP}-Pad19)
- U1741 pad 20: (no net) -> unconnected-(U1741-~{LD_DET}-Pad20)
- U1741 pad 5: SYS_3V3 -> /SYS_3V3
- U1742 pad 1: (no net) -> unconnected-(U1742-NC-Pad1)
- U1742 pad 13: SYS_3V3 -> /SYS_3V3
- U1742 pad 18: (no net) -> unconnected-(U1742-NC-Pad18)
- U1742 pad 2: (no net) -> unconnected-(U1742-NC-Pad2)
- U1742 pad 20: SYS_3V3 -> /SYS_3V3
- U1742 pad 3: (no net) -> unconnected-(U1742-NC-Pad3)
- U1742 pad 30: SYS_3V3 -> /SYS_3V3
- U1742 pad 31: (no net) -> unconnected-(U1742-HSB(p)-Pad31)
- U1742 pad 32: (no net) -> unconnected-(U1742-HSB(n)-Pad32)
- U1742 pad 33: (no net) -> unconnected-(U1742-HSC(p)-Pad33)
- U1742 pad 34: (no net) -> unconnected-(U1742-HSC(n)-Pad34)
- U1742 pad 35: (no net) -> unconnected-(U1742-NC-Pad35)
- U1742 pad 36: (no net) -> unconnected-(U1742-NC-Pad36)
- U1742 pad 37: (no net) -> unconnected-(U1742-NC-Pad37)
- U1742 pad 38: (no net) -> unconnected-(U1742-NC-Pad38)
- U1742 pad 39: (no net) -> unconnected-(U1742-NC-Pad39)
- U1742 pad 4: (no net) -> unconnected-(U1742-NC-Pad4)
- U1742 pad 40: (no net) -> unconnected-(U1742-NC-Pad40)
- U1742 pad 41: (no net) -> unconnected-(U1742-NC-Pad41)
- U1742 pad 42: (no net) -> unconnected-(U1742-NC-Pad42)
- U1742 pad 5: (no net) -> unconnected-(U1742-NC-Pad5)
- U1742 pad 7: (no net) -> unconnected-(U1742-HSA(n)-Pad7)
- U1742 pad 8: (no net) -> unconnected-(U1742-HSA(p)-Pad8)
- U1745 pad 10: (no net) -> unconnected-(U1745-NC-Pad10)
- U1745 pad 6: (no net) -> unconnected-(U1745-NC-Pad6)
- U1745 pad 7: (no net) -> unconnected-(U1745-NC-Pad7)
- U1745 pad 9: (no net) -> unconnected-(U1745-NC-Pad9)
- U1780 pad 1: USB_PORT_5V -> /USB_PORT_5V
- U1781 pad 16: (no net) -> unconnected-(U1781-~{DEBUG}-Pad16)
- U1781 pad 17: (no net) -> unconnected-(U1781-~{AUDIO}-Pad17)
- U1781 pad 19: (no net) -> unconnected-(U1781-~{UFP}-Pad19)
- U1781 pad 20: (no net) -> unconnected-(U1781-~{LD_DET}-Pad20)
- U1781 pad 5: SYS_3V3 -> /SYS_3V3
- U1782 pad 1: (no net) -> unconnected-(U1782-NC-Pad1)
- U1782 pad 13: SYS_3V3 -> /SYS_3V3
- U1782 pad 18: (no net) -> unconnected-(U1782-NC-Pad18)
- U1782 pad 2: (no net) -> unconnected-(U1782-NC-Pad2)
- U1782 pad 20: SYS_3V3 -> /SYS_3V3
- U1782 pad 3: (no net) -> unconnected-(U1782-NC-Pad3)
- U1782 pad 30: SYS_3V3 -> /SYS_3V3
- U1782 pad 31: (no net) -> unconnected-(U1782-HSB(p)-Pad31)
- U1782 pad 32: (no net) -> unconnected-(U1782-HSB(n)-Pad32)
- U1782 pad 33: (no net) -> unconnected-(U1782-HSC(p)-Pad33)
- U1782 pad 34: (no net) -> unconnected-(U1782-HSC(n)-Pad34)
- U1782 pad 35: (no net) -> unconnected-(U1782-NC-Pad35)
- U1782 pad 36: (no net) -> unconnected-(U1782-NC-Pad36)
- U1782 pad 37: (no net) -> unconnected-(U1782-NC-Pad37)
- U1782 pad 38: (no net) -> unconnected-(U1782-NC-Pad38)
- U1782 pad 39: (no net) -> unconnected-(U1782-NC-Pad39)
- U1782 pad 4: (no net) -> unconnected-(U1782-NC-Pad4)
- U1782 pad 40: (no net) -> unconnected-(U1782-NC-Pad40)
- U1782 pad 41: (no net) -> unconnected-(U1782-NC-Pad41)
- U1782 pad 42: (no net) -> unconnected-(U1782-NC-Pad42)
- U1782 pad 5: (no net) -> unconnected-(U1782-NC-Pad5)
- U1782 pad 7: (no net) -> unconnected-(U1782-HSA(n)-Pad7)
- U1782 pad 8: (no net) -> unconnected-(U1782-HSA(p)-Pad8)
- U1785 pad 10: (no net) -> unconnected-(U1785-NC-Pad10)
- U1785 pad 6: (no net) -> unconnected-(U1785-NC-Pad6)
- U1785 pad 7: (no net) -> unconnected-(U1785-NC-Pad7)
- U1785 pad 9: (no net) -> unconnected-(U1785-NC-Pad9)
- U1800 pad 1: USB_PORT_5V -> /USB_PORT_5V
- U1800 pad 3: INTERNAL_USB_VBUS_VALID -> /INTERNAL_USB_VBUS_VALID
- U1800 pad 4: (no net) -> unconnected-(U1800-~{FAULT}-Pad4)
- U1802 pad 10: (no net) -> unconnected-(U1802-NC-Pad10)
- U1802 pad 6: (no net) -> unconnected-(U1802-NC-Pad6)
- U1802 pad 7: (no net) -> unconnected-(U1802-NC-Pad7)
- U1802 pad 9: (no net) -> unconnected-(U1802-NC-Pad9)
- U1803 pad 1: USB_PORT_5V -> /USB_PORT_5V
- U1803 pad 3: INTERNAL_USB_VBUS_VALID -> /INTERNAL_USB_VBUS_VALID
- U1803 pad 4: (no net) -> unconnected-(U1803-~{FAULT}-Pad4)
- U2000 pad 1: SYS_3V3 -> /SYS_3V3
- U2000 pad 10: (no net) -> unconnected-(U2000-RSVD2-Pad10)
- U2000 pad 11: (no net) -> unconnected-(U2000-NC-Pad11)
- U2000 pad 12: (no net) -> unconnected-(U2000-RSVD3-Pad12)
- U2000 pad 13: (no net) -> unconnected-(U2000-RSVD4-Pad13)
- U2000 pad 15: USBC1_SSTX_N -> /USBC1_SSTX_N
- U2000 pad 16: USBC1_SSTX_P -> /USBC1_SSTX_P
- U2000 pad 20: SYS_3V3 -> /SYS_3V3
- U2000 pad 23: (no net) -> unconnected-(U2000-AEQCFG-Pad23)
- U2000 pad 24: (no net) -> unconnected-(U2000-NC-Pad24)
- U2000 pad 25: (no net) -> unconnected-(U2000-NC-Pad25)
- U2000 pad 28: SYS_3V3 -> /SYS_3V3
- U2000 pad 29: (no net) -> unconnected-(U2000-CEQ1-Pad29)
- U2000 pad 32: (no net) -> unconnected-(U2000-NC-Pad32)
- U2000 pad 35: (no net) -> unconnected-(U2000-SSEQ0/A0-Pad35)
- U2000 pad 38: (no net) -> unconnected-(U2000-CEQ0-Pad38)
- U2000 pad 5: (no net) -> unconnected-(U2000-NC-Pad5)
- U2000 pad 6: SYS_3V3 -> /SYS_3V3
- U2000 pad 7: (no net) -> unconnected-(U2000-TESTOUT1-Pad7)
- U2000 pad 8: (no net) -> unconnected-(U2000-TESTOUT2-Pad8)
- U2000 pad 9: (no net) -> unconnected-(U2000-RSVD1-Pad9)
- U2001 pad 16: (no net) -> unconnected-(U2001-NC-Pad16)
- U2001 pad 17: (no net) -> unconnected-(U2001-NC-Pad17)
- U2001 pad 19: (no net) -> unconnected-(U2001-NC-Pad19)
- U2001 pad 20: (no net) -> unconnected-(U2001-NC-Pad20)
- U2003 pad 10: SYS_3V3 -> /SYS_3V3
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
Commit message: get the main boards ready for routing
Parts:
- C1852: value 100n C0G USB3-A SSTX+ series AC -> 100n 16V X7R USB3-A SSTX+ series AC
- C1853: value 100n C0G USB3-A SSTX- series AC -> 100n 16V X7R USB3-A SSTX- series AC
- moved R2082 151.7 mm to (51.6, 32.2), turned to -90 degrees
- moved C1713 151.5 mm to (22.6, 25.3), turned to 90 degrees
- moved C2081 151.5 mm to (54.9, 26.8)
- moved C2142 141.7 mm to (39.0, 42.8), turned to 90 degrees
- moved R2142 133.4 mm to (32.5, 48.4), turned to 180 degrees
- moved C2025 132.3 mm to (35.6, 37.3), turned to -90 degrees
- moved C2143 131.4 mm to (42.4, 49.1)
- moved R2002 129.8 mm to (61.5, 33.4), turned to -90 degrees
- moved C2026 125.7 mm to (46.1, 37.3), turned to -90 degrees
- moved C2007 122.8 mm to (12.7, 27.2), turned to 90 degrees
- moved C2146 120.6 mm to (42.9, 54.6), turned to -90 degrees
- moved C2030 118.7 mm to (24.0, 19.3)
- moved C1834 112.4 mm to (58.1, 85.7), turned to 180 degrees
- moved U1701 110.7 mm to (45.0, 118.0)
- moved C2003 109.3 mm to (23.2, 36.0)
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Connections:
- net /HUB_DS1_DM renamed /HUB_DS1_DN
- net /HUB_DS4_DM renamed /HUB_DS4_DN
- net /PD1 Dual-Role/PD1_DM_CONN renamed /PD1 Dual-Role/PD1_CONN_DN
- net /PD1 Dual-Role/PD1_DM_HOST_SWITCHED renamed /PD1 Dual-Role/PD1_HOST_SWITCHED_DN
- net /PD1 Dual-Role/PD1_DP_CONN renamed /PD1 Dual-Role/PD1_CONN_DP
- net /PD1 Dual-Role/PD1_DP_HOST_SWITCHED renamed /PD1 Dual-Role/PD1_HOST_SWITCHED_DP
- net /USB Hub + Ports/HUB_DIS5_DM renamed /USB Hub + Ports/HUB_DIS5_DN
- net /USB Hub + Ports/HUB_DIS6_DM renamed /USB Hub + Ports/HUB_DIS6_DN
- net /USB Hub + Ports/HUB_DS2_DM renamed /USB Hub + Ports/HUB_DS2_DN
- net /USB Hub + Ports/HUB_DS3_DM renamed /USB Hub + Ports/HUB_DS3_DN
- net /USBC1_DM renamed /USBC1_DN
- net /USBC2_DM renamed /USBC2_DN
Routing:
- net /USB Hub + Ports/J24_5V_PRE: track 0.00 -> 17.7 mm
- net /USB Hub + Ports/J23_TX2_P: track 0.00 -> 14.1 mm
- net /USB Hub + Ports/J23_RX1_N: track 0.00 -> 13.4 mm
- net /USB Hub + Ports/J23_RX1_P: track 0.00 -> 12.2 mm
- net /USB Hub + Ports/J23_TX2_N: track 0.00 -> 11.4 mm
- net GND: track 0.00 -> 9.59 mm
- net /USB Hub + Ports/J23_RX2_N: track 0.00 -> 9.58 mm
- net /USB Hub + Ports/J23_RX2_P: track 0.00 -> 9.02 mm
- net /USB Hub + Ports/J23_TX1_N: track 0.00 -> 8.70 mm
- net /USB Hub + Ports/HUB_DIS5_TX_P: track 0.00 -> 7.15 mm
- net /USB Hub + Ports/J23_TX1_P: track 0.00 -> 6.09 mm
- net /USB Hub + Ports/J25_5V_PRE: track 0.00 -> 5.29 mm
- net /USB Hub + Ports/HUB_DIS6_DP: track 0.00 -> 4.56 mm
- net /USB Hub + Ports/HUB_DIS6_DN: track 0.00 -> 4.52 mm
- net /USB Hub + Ports/HUB_DS3_DP: track 0.00 -> 3.96 mm
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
